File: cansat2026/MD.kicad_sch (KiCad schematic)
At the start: 6 parts, among them J401 M_Power_Conn, J402 M1, J403 M2, U401 DRV8835

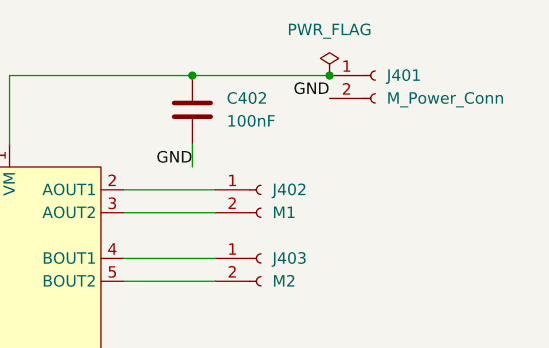
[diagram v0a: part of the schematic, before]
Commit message: Update: MCUシートを作成
MCU部分を分けた
あとでFPGAつけるかもしれないしね
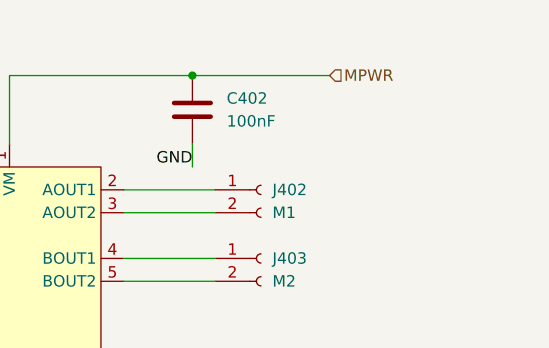
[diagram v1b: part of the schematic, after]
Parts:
- removed J401: M_Power_Conn, Connector_JST:JST_XH_B2B-XH-A_1x02_P2.50mm_Vertical, symbol Connector:Conn_01x02_Socket
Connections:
- net MPWR: now reaches C402.1, U401.1 (VM)
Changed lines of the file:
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@@
-	)
-	(junction
-		(at 177.8 81.28)
-		(diameter 0)
-		(color 0 0 0 0)
 	)
 	(junction
@@
 	)
 	(label "GND"
-		(at 177.8 83.82 180)
-		(effects
-			(font
-				(size 1.27 1.27)
-			)
-			(justify right bottom)
-		)
-	)
-	(label "GND"
 		(at 162.56 91.44 180)
 		(effects
@@
 		)
 	)
+	(hierarchical_label "MPWR"
+		(shape input)
+		(at 177.8 81.28 0)
+		(effects
+			(font
+				(size 1.27 1.27)
+			)
+			(justify left)
+		)
+	)
 	(hierarchical_label "BIN2"
 		(shape input)
@@
 			)
 			(justify right)
-		)
-	)
-	(symbol
-		(lib_id "power:PWR_FLAG")
-		(at 177.8 81.28 0)
-		(unit 1)
-		(body_style 1)
-		(exclude_from_sim no)
-		(in_bom yes)
-		(on_board yes)
-		(in_pos_files yes)
-		(dnp no)
-		(fields_autoplaced yes)
-		(property "Reference" "#FLG0401"
-			(at 177.8 79.375 0)
-			(hide yes)
-			(show_name no)
-			(do_not_autoplace no)
-			(effects
-				(font
-					(size 1.27 1.27)
-				)
-			)
-		)
-		(property "Value" "PWR_FLAG"
-			(at 177.8 76.2 0)
-			(show_name no)
-			(do_not_autoplace no)
-			(effects
-				(font
-					(size 1.27 1.27)
-				)
-			)
-		)
-		(property "Footprint" ""
-			(at 177.8 81.28 0)
-			(hide yes)
-			(show_name no)
-			(do_not_autoplace no)
-			(effects
-				(font
-					(size 1.27 1.27)
-				)
-			)
-		)
-		(property "Datasheet" ""
-			(at 177.8 81.28 0)
-			(hide yes)
-			(show_name no)
-			(do_not_autoplace no)
-			(effects
-				(font
-					(size 1.27 1.27)
-				)
-			)
-		)
-		(property "Description" "Special symbol for telling ERC where power comes from"
-			(at 177.8 81.28 0)
-			(hide yes)
-			(show_name no)
-			(do_not_autoplace no)
-			(effects
-				(font
-					(size 1.27 1.27)
-				)
-			)
-		)
-		(pin "1"
-		)
-		(instances
-			(project cansat2026
-				(path "/bf092721-05bb-4932-a328-528d8d2db6b5/677c7cab-135e-4675-a1c6-e0f4681489b7"
-					(reference "#FLG0401")
-					(unit 1)
-				)
-			)
 		)
 	)
@@
 		)
 		(instances
-			(project cansat2026
+			(project "cansat2026"
 				(path "/bf092721-05bb-4932-a328-528d8d2db6b5/677c7cab-135e-4675-a1c6-e0f4681489b7"
 					(reference "J403")
-					(unit 1)
-				)
-			)
-		)
-	)
-	(symbol
-		(lib_id "Connector:Conn_01x02_Socket")
-		(at 182.88 81.28 0)
-		(unit 1)
-		(body_style 1)
-		(exclude_from_sim no)
-		(in_bom yes)
-		(on_board yes)
-		(in_pos_files yes)
-		(dnp no)
-		(fields_autoplaced yes)
-		(property "Reference" "J401"
-			(at 184.15 81.2799 0)
-			(show_name no)
-			(do_not_autoplace no)
-			(effects
-				(font
-					(size 1.27 1.27)
-				)
-				(justify left)
-			)
-		)
-		(property "Value" "M_Power_Conn"
-			(at 184.15 83.8199 0)
-			(show_name no)
-			(do_not_autoplace no)
-			(effects
-				(font
-					(size 1.27 1.27)
-				)
-				(justify left)
-			)
-		)
-		(property "Footprint" "Connector_JST:JST_XH_B2B-XH-A_1x02_P2.50mm_Vertical"
-			(at 182.88 81.28 0)
-			(hide yes)
-			(show_name no)
-			(do_not_autoplace no)
-			(effects
-				(font
-					(size 1.27 1.27)
-				)
-			)
-		)
-		(property "Datasheet" ""
-			(at 182.88 81.28 0)
-			(hide yes)
-			(show_name no)
-			(do_not_autoplace no)
-			(effects
-				(font
-					(size 1.27 1.27)
-				)
-			)
-		)
-		(property "Description" "Generic connector, single row, 01x02, script generated"
-			(at 182.88 81.28 0)
-			(hide yes)
-			(show_name no)
-			(do_not_autoplace no)
-			(effects
-				(font
-					(size 1.27 1.27)
-				)
-			)
-		)
-		(property "LCSC Part" ""
-			(at 182.88 81.28 0)
-			(hide yes)
-			(show_name no)
-			(do_not_autoplace no)
-			(effects
-				(font
-					(size 1.27 1.27)
-				)
-			)
-		)
-		(property "Mouser Part" ""
-			(at 182.88 81.28 0)
-			(hide yes)
-			(show_name no)
-			(do_not_autoplace no)
-			(effects
-				(font
-					(size 1.27 1.27)
-				)
-			)
-		)
-		(pin "1"
-		)
-		(pin "2"
-		)
-		(instances
-			(project cansat2026
-				(path "/bf092721-05bb-4932-a328-528d8d2db6b5/677c7cab-135e-4675-a1c6-e0f4681489b7"
-					(reference "J401")
 					(unit 1)
 				)
@@
 		)
 		(instances
-			(project cansat2026
+			(project "cansat2026"
 				(path "/bf092721-05bb-4932-a328-528d8d2db6b5/677c7cab-135e-4675-a1c6-e0f4681489b7"
 					(reference "U401")
@@
 		)
 		(instances
-			(project cansat2026
+			(project "cansat2026"
 				(path "/bf092721-05bb-4932-a328-528d8d2db6b5/677c7cab-135e-4675-a1c6-e0f4681489b7"
 					(reference "J402")
@@
 		)
 		(instances
-			(project cansat2026
+			(project "cansat2026"
 				(path "/bf092721-05bb-4932-a328-528d8d2db6b5/677c7cab-135e-4675-a1c6-e0f4681489b7"
 					(reference "C401")
@@
 		)
 		(instances
-			(project cansat2026
+			(project "cansat2026"
 				(path "/bf092721-05bb-4932-a328-528d8d2db6b5/677c7cab-135e-4675-a1c6-e0f4681489b7"
 					(reference "C402")

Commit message: Update: いろいろした
無線変えた
カメラのコネクタ変えた
i2cセンサ変えた
電源変えた:1.2V,3.8V,3.3V
IOエキスパンダ追加
FPGA追加
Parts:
- renumbered J402 to J401, J403 to J402
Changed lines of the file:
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@@
 		(dnp no)
 		(fields_autoplaced yes)
-		(property "Reference" "J403"
+		(property "Reference" "J402"
 			(at 171.45 101.5999 0)
 			(show_name no)
@@
 		)
 		(property "Mouser Part" ""
+			(at 170.18 101.6 0)
+			(hide yes)
+			(show_name no)
+			(do_not_autoplace no)
+			(effects
+				(font
+					(size 1.27 1.27)
+				)
+			)
+		)
+		(property "DigiKey Part" ""
 			(at 170.18 101.6 0)
 			(hide yes)
@@
 			(project "cansat2026"
 				(path "/bf092721-05bb-4932-a328-528d8d2db6b5/677c7cab-135e-4675-a1c6-e0f4681489b7"
-					(reference "J403")
+					(reference "J402")
 					(unit 1)
 				)
@@
 			)
 		)
+		(property "DigiKey Part" ""
+			(at 139.7 101.6 0)
+			(hide yes)
+			(show_name no)
+			(do_not_autoplace no)
+			(effects
+				(font
+					(size 1.27 1.27)
+				)
+			)
+		)
 		(pin "3"
 		)
@@
 		(in_pos_files yes)
 		(dnp no)
-		(property "Reference" "J402"
+		(property "Reference" "J401"
 			(at 171.45 93.9799 0)
 			(show_name no)
@@
 		)
 		(property "Mouser Part" ""
+			(at 170.18 93.98 0)
+			(hide yes)
+			(show_name no)
+			(do_not_autoplace no)
+			(effects
+				(font
+					(size 1.27 1.27)
+				)
+			)
+		)
+		(property "DigiKey Part" ""
 			(at 170.18 93.98 0)
 			(hide yes)
@@
 			(project "cansat2026"
 				(path "/bf092721-05bb-4932-a328-528d8d2db6b5/677c7cab-135e-4675-a1c6-e0f4681489b7"
-					(reference "J402")
+					(reference "J401")
 					(unit 1)
 				)
@@
 			)
 		)
+		(property "DigiKey Part" ""
+			(at 116.84 85.09 0)
+			(hide yes)
+			(show_name no)
+			(do_not_autoplace no)
+			(effects
+				(font
+					(size 1.27 1.27)
+				)
+			)
+		)
 		(pin "1"
 		)
@@
 			(at 162.56 85.09 0)
 			(hide yes)
+			(show_name no)
+			(do_not_autoplace no)
+			(effects
+				(font
+					(size 1.27 1.27)
+				)
+			)
+		)
+		(property "DigiKey Part" ""
+			(at 162.56 85.09 0)
+			(hide yes)

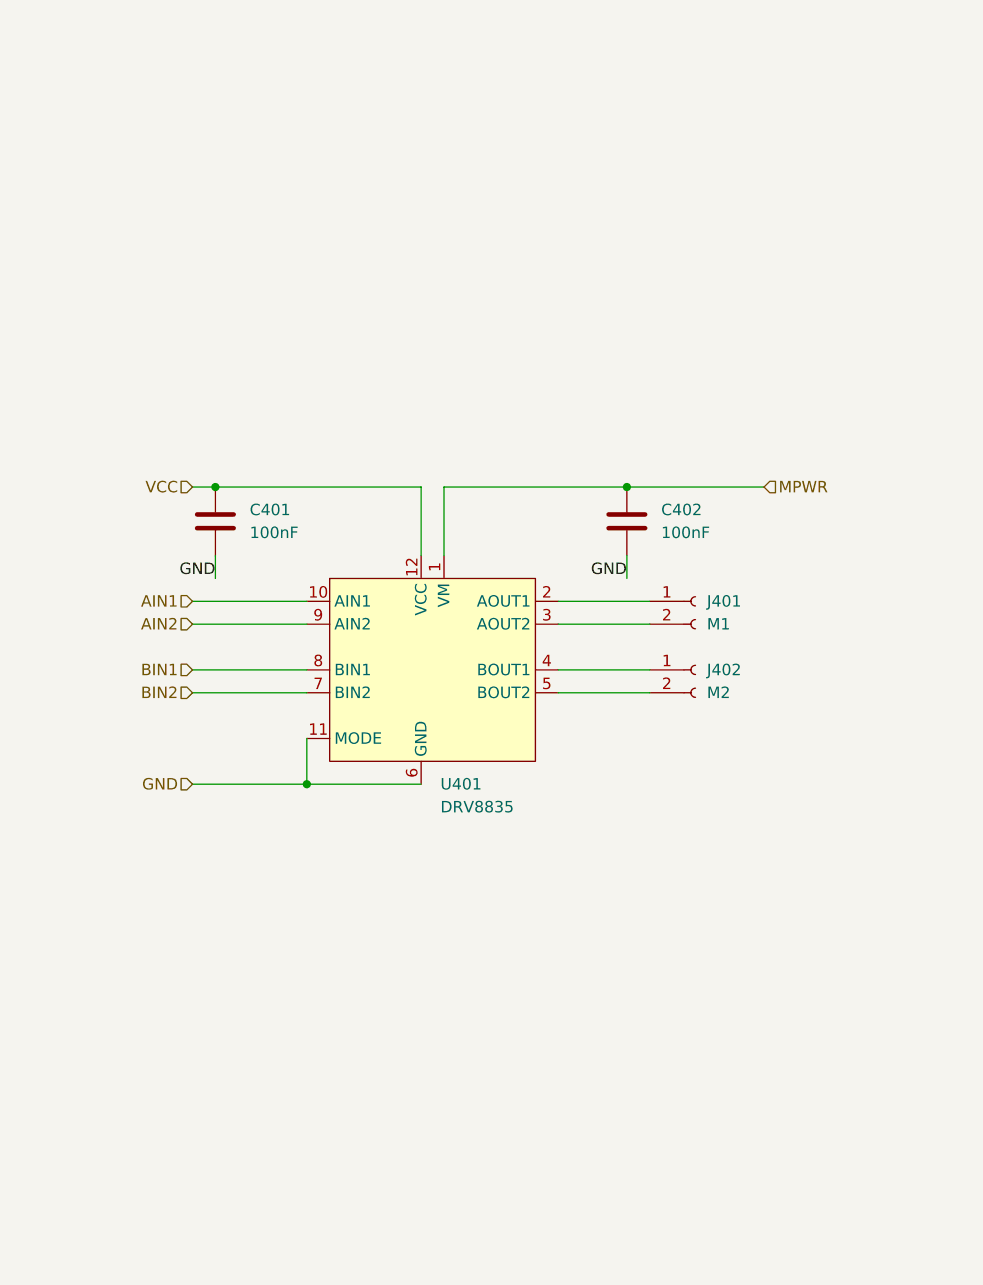
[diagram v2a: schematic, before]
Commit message: Update: MDと電源とか
MD変えた
モーター電源と主電源
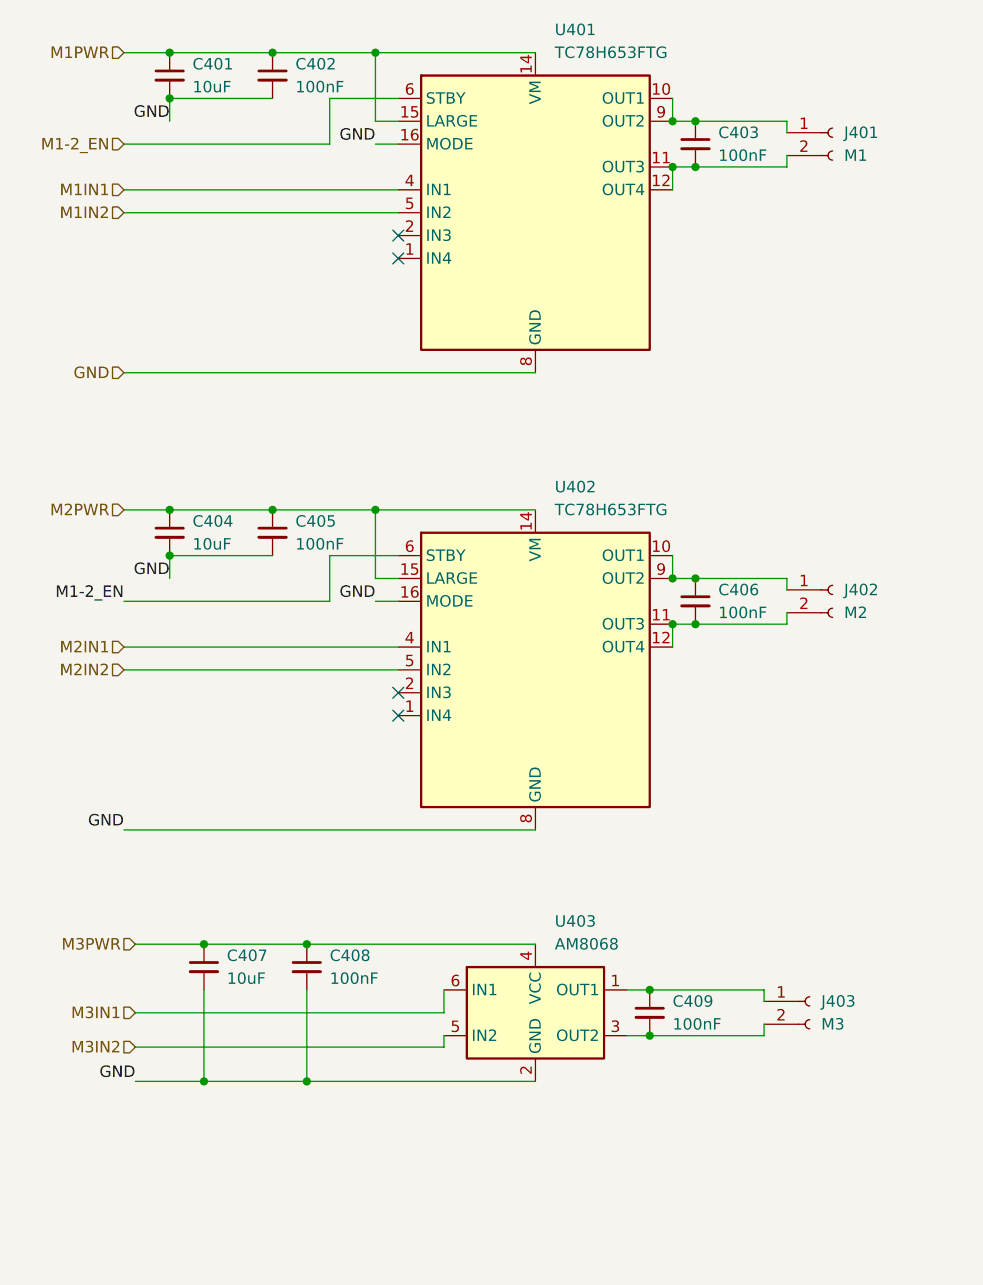
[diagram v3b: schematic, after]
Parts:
- removed C401, C402: 100nF, Capacitor_SMD:C_0402_1005Metric, symbol Device:C
- removed U401: DRV8835, Package_SON:WSON-12-1EP_3x2mm_P0.5mm_EP1x2.65_ThermalVias, symbol Project:DRV8835
- added C401, C404, C407: 10uF, Capacitor_SMD:C_0805_2012Metric, symbol Device:C_Small
- added C402, C403, C405, C406, C408, C409: 100nF, Capacitor_SMD:C_0402_1005Metric, symbol Device:C_Small
- added J403: M3, Connector_JST:JST_XH_B2B-XH-A_1x02_P2.50mm_Vertical, symbol Connector:Conn_01x02_Socket
- added U401, U402: TC78H653FTG, Package_DFN_QFN:VQFN-16-1EP_3x3mm_P0.5mm_EP1.8x1.8mm, symbol Project:TC78H653FTG
- added U403: AM8068, Package_TO_SOT_SMD:SOT-23-6, symbol Project:AM8068
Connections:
- net GND: now also C401.2, C402.2, C404.2, C405.2, C407.2, C408.2, U401.13 (GND), U401.16 (MODE), U401.8 (GND), U402.13 (GND), U402.16 (MODE), U402.8 (GND), U403.2 (GND)
- net at J402.1 (Pin_1): now also C406.1, U402.10 (OUT1), U402.9 (OUT2)
- net at J402.2 (Pin_2): now also C406.2, U402.11 (OUT3), U402.12 (OUT4)
- net at J401.1 (Pin_1): now also C403.1, U401.10 (OUT1), U401.9 (OUT2)
- net at J401.2 (Pin_2): now also C403.2, U401.11 (OUT3), U401.12 (OUT4)
- new net: C409.1, J403.1 (Pin_1), U403.1 (OUT1)
- new net: C409.2, J403.2 (Pin_2), U403.3 (OUT2)
- new net: U402.3 (NC), U402.7 (NC)
- new net: U401.3 (NC), U401.7 (NC)
- new net M1-2_EN: U401.6 (STBY), U402.6 (STBY)
- new net M1IN1: U401.4 (IN1)
- new net M1IN2: U401.5 (IN2)
- new net M1PWR: C401.1, C402.1, U401.14 (VM), U401.15 (LARGE)
- new net M2IN1: U402.4 (IN1)
- new net M2IN2: U402.5 (IN2)
- new net M2PWR: C404.1, C405.1, U402.14 (VM), U402.15 (LARGE)
- new net M3IN1: U403.6 (IN1)
- new net M3IN2: U403.5 (IN2)
- new net M3PWR: C407.1, C408.1, U403.4 (VCC)
- no-connect marks 0 -> 4

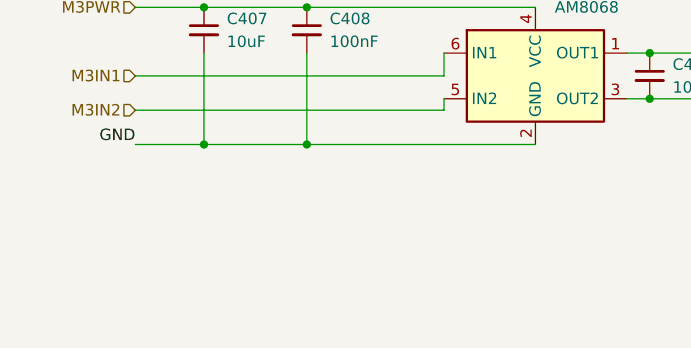
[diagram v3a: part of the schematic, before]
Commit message: Update: いろいろした
GPS変えた
USB追加した
気圧センサ変えた
FPGA変えた
MDにキャパシタ追加した
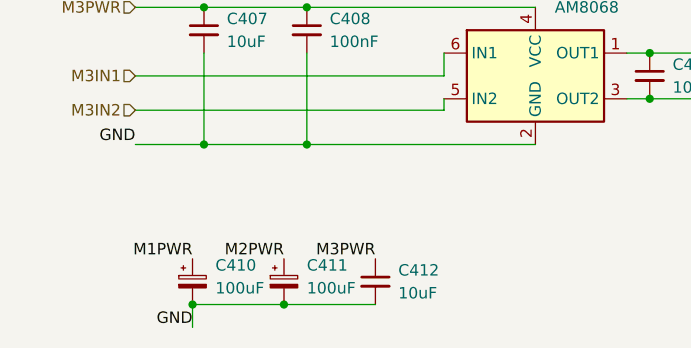
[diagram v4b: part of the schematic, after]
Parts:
- added C410, C411: 100uF, Capacitor_THT:CP_Radial_D6.3mm_P2.50mm, symbol Device:C_Polarized_Small
- added C412: 10uF, Capacitor_SMD:C_0805_2012Metric, symbol Device:C_Small
- U401, U402: LCSC Part (none) -> C37313337
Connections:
- net GND: now also U401.17 (GND), U402.17 (GND), C410.2, C411.2, C412.2
- net M1PWR: now also C410.1
- net M2PWR: now also C411.1
- net M3PWR: now also C412.1

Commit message: Update: 完成した
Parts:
- C401, C404, C407, C412: footprint Capacitor_SMD:C_0805_2012Metric -> Capacitor_SMD:C_0603_1608Metric; LCSC Part C15850 -> C19702
- J401, J402: footprint Connector_JST:JST_XH_B2B-XH-A_1x02_P2.50mm_Vertical -> Connector_JST:JST_VH_B2P-VH_1x02_P3.96mm_Vertical; 秋月 Part (none) -> 112815
- J403: 秋月 Part (none) -> 112247
- U403: 秋月 Part (none) -> 118301
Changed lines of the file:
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@@
+			)
+		)
+		(property "秋月 Part" "118301"
+			(at 152.4 139.7 0)
+			(hide yes)
+			(show_name no)
+			(do_not_autoplace no)
+			(effects
+				(font
+					(size 1.27 1.27)
+				)
 			)
 		)
@@
 			)
 		)
+		(property "秋月 Part" "112247"
+			(at 182.88 138.43 0)
+			(hide yes)
+			(show_name no)
+			(do_not_autoplace no)
+			(effects
+				(font
+					(size 1.27 1.27)
+				)
+			)
+		)
 		(pin "1"
 		)
@@
 			)
 		)
-		(property "Footprint" "Connector_JST:JST_XH_B2B-XH-A_1x02_P2.50mm_Vertical"
+		(property "Footprint" "Connector_JST:JST_VH_B2P-VH_1x02_P3.96mm_Vertical"
 			(at 185.42 92.71 0)
 			(hide yes)
@@
 		)
 		(property "DigiKey Part" ""
+			(at 185.42 92.71 0)
+			(hide yes)
+			(show_name no)
+			(do_not_autoplace no)
+			(effects
+				(font
+					(size 1.27 1.27)
+				)
+			)
+		)
+		(property "秋月 Part" "112815"
 			(at 185.42 92.71 0)
 			(hide yes)
@@
 			)
 		)
-		(property "Footprint" "Connector_JST:JST_XH_B2B-XH-A_1x02_P2.50mm_Vertical"
+		(property "Footprint" "Connector_JST:JST_VH_B2P-VH_1x02_P3.96mm_Vertical"
 			(at 185.42 41.91 0)
 			(hide yes)
@@
 		)
 		(property "DigiKey Part" ""
+			(at 185.42 41.91 0)
+			(hide yes)
+			(show_name no)
+			(do_not_autoplace no)
+			(effects
+				(font
+					(size 1.27 1.27)
+				)
+			)
+		)
+		(property "秋月 Part" "112815"
 			(at 185.42 41.91 0)
 			(hide yes)
@@
 			)
 		)
-		(property "Footprint" "Capacitor_SMD:C_0805_2012Metric"
+		(property "Footprint" "Capacitor_SMD:C_0603_1608Metric"
 			(at 111.76 86.36 0)
 			(hide yes)
@@
 			)
 		)
-		(property "LCSC Part" "C15850"
+		(property "LCSC Part" "C19702"
 			(at 111.76 86.36 0)
 			(hide yes)
@@
 			)
 		)
-		(property "Footprint" "Capacitor_SMD:C_0805_2012Metric"
+		(property "Footprint" "Capacitor_SMD:C_0603_1608Metric"
 			(at 111.76 35.56 0)
 			(hide yes)
@@
 			)
 		)
-		(property "LCSC Part" "C15850"
+		(property "LCSC Part" "C19702"
 			(at 111.76 35.56 0)
 			(hide yes)
@@
 			)
 		)
-		(property "Footprint" "Capacitor_SMD:C_0805_2012Metric"
+		(property "Footprint" "Capacitor_SMD:C_0603_1608Metric"
 			(at 134.62 162.56 0)
 			(hide yes)
@@
 			)
 		)
-		(property "LCSC Part" "C15850"
+		(property "LCSC Part" "C19702"
 			(at 134.62 162.56 0)
 			(hide yes)
@@
 			)
 		)
-		(property "Footprint" "Capacitor_SMD:C_0805_2012Metric"
+		(property "Footprint" "Capacitor_SMD:C_0603_1608Metric"
 			(at 115.57 134.62 0)
 			(hide yes)
@@
 			)
 		)
-		(property "LCSC Part" "C15850"
+		(property "LCSC Part" "C19702"
 			(at 115.57 134.62 0)
 			(hide yes)
